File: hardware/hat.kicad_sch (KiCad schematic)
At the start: 41 parts

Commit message: schematic
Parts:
- C101: value (none) -> DSK-3R3H334T-HL; footprint (none) -> kicad-libraries:DSK
- C102, C103, C109, C111: value (none) -> 100nF; footprint (none) -> kicad-libraries:C0603F
- C104, C105, C106, C114, C115: value (none) -> 1uF; footprint (none) -> kicad-libraries:C0603F
- C107, C108, C110, C112, C113: value (none) -> 10uF; footprint (none) -> kicad-libraries:C1206
- C116, C117: value (none) -> DNP; footprint (none) -> kicad-libraries:C0402F
- D101: value (none) -> BAQ33-GS08; footprint (none) -> kicad-libraries:MiniMelf
- D102: value (none) -> blue; footprint (none) -> kicad-libraries:D0603F
- J101: value (none) -> Raspberry_Pi_2_3; footprint (none) -> kicad-libraries:raspberrypi_hat2
- J102: value (none) -> Boot; footprint (none) -> kicad-libraries:SolderJumper
- L101, L102: value (none) -> 742792040; footprint (none) -> kicad-libraries:R0805
- P101: value (none) -> Debug; footprint (none) -> kicad-libraries:DEBUG_PAD
- R101, R102, R103, R104, R106: value (none) -> 1k; footprint (none) -> kicad-libraries:R0603F
- R105: value (none) -> 68; footprint (none) -> kicad-libraries:R0603F
- RP101, RP105: value (none) -> 3.9k; footprint (none) -> kicad-libraries:4X0402
- RP102, RP103, RP104: value (none) -> 82; footprint (none) -> kicad-libraries:4X0402
- U101: value (none) -> XMC1100; footprint (none) -> QFN24-4x4mm-0.5mm
- U102: value (none) -> LD1117; footprint (none) -> kicad-libraries:SOT-223
- U103, U104: value (none) -> TPS22975; footprint (none) -> WSON8-2x2
- U105: value (none) -> PCF8523T; footprint (none) -> kicad-libraries:SO-8
- X101: value (none) -> 32.768kHz; footprint (none) -> kicad-libraries:AB26TRQ
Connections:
- net PowerGood: now reaches U101.20 (P0.9_IO)
- no-connect marks 26 -> 25
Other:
- note added: "Copyright Tinkerforge GmbH 2023. This documentation describes Open Hardware and is licensed under the CERN OHL v. 1.1. You may redistribute and modify this documentation under the terms of the CERN OHL v.1.1. (http://ohwr.org/cernohl). This documentation is distributed WITHOUT ANY EXPRESS OR IMPLIED WARRANTY, INCLUDING OF MERCHANTABILITY, SATISFACTORY QUALITY AND FITNESS FOR A PARTICULAR PURPOSE.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"
- note removed: "Copyright Tinkerforge GmbH 2021. This documentation describes Open Hardware and is licensed under the CERN OHL v. 1.1. You may redistribute and modify this documentation under the terms of the CERN OHL v.1.1. (http://ohwr.org/cernohl). This documentation is distributed WITHOUT ANY EXPRESS OR IMPLIED WARRANTY, INCLUDING OF MERCHANTABILITY, SATISFACTORY QUALITY AND FITNESS FOR A PARTICULAR PURPOSE.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"

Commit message: Proto V1.8
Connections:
- net GND: now also U101.16 (P0.5_IO)
- net PowerGood: now also U101.6 (P2.9_AI); no longer U101.20 (P0.9_IO)
- no-connect marks 25 -> 24
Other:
- note added: "Version Detect V1.8"

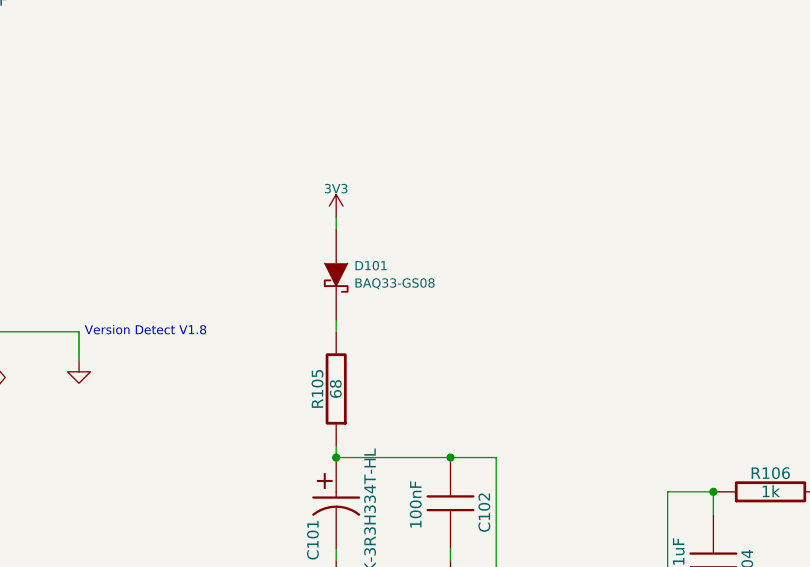
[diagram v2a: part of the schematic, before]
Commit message: changed D101
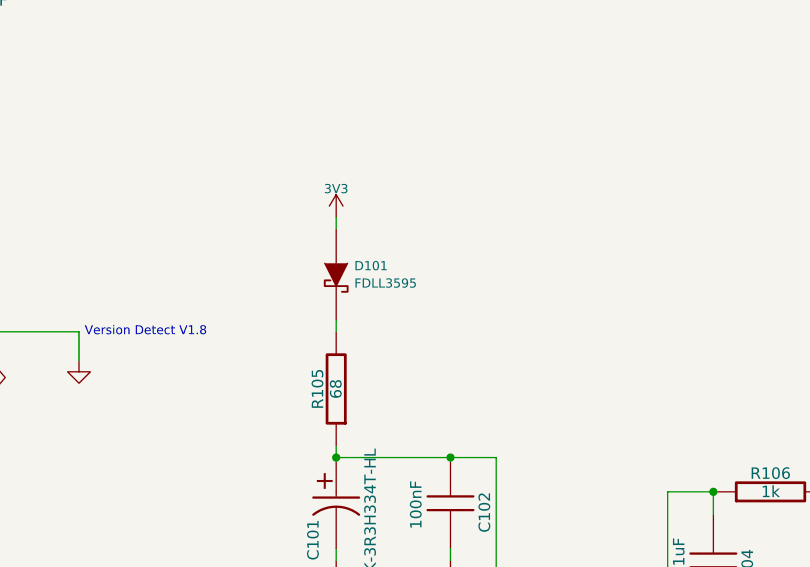
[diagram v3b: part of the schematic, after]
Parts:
- D101: value BAQ33-GS08 -> FDLL3595
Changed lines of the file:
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@@
       (effects (font (size 1.016 1.016)) (justify left))
     )
-    (property "Value" "BAQ33-GS08" (id 1) (at 94.7166 61.9252 90)
+    (property "Value" "FDLL3595" (id 1) (at 94.7166 61.9252 90)
       (effects (font (size 1.016 1.016)) (justify left))
     )
@@
     )
     (path "/00000000-0000-0000-0000-00005c8db5e2"
-      (reference "D101") (unit 1) (value "BAQ33-GS08") (footprint "kicad-libraries:MiniMelf")
+      (reference "D101") (unit 1) (value "FDLL3595") (footprint "kicad-libraries:MiniMelf")
     )
     (path "/00000000-0000-0000-0000-00005b476059"

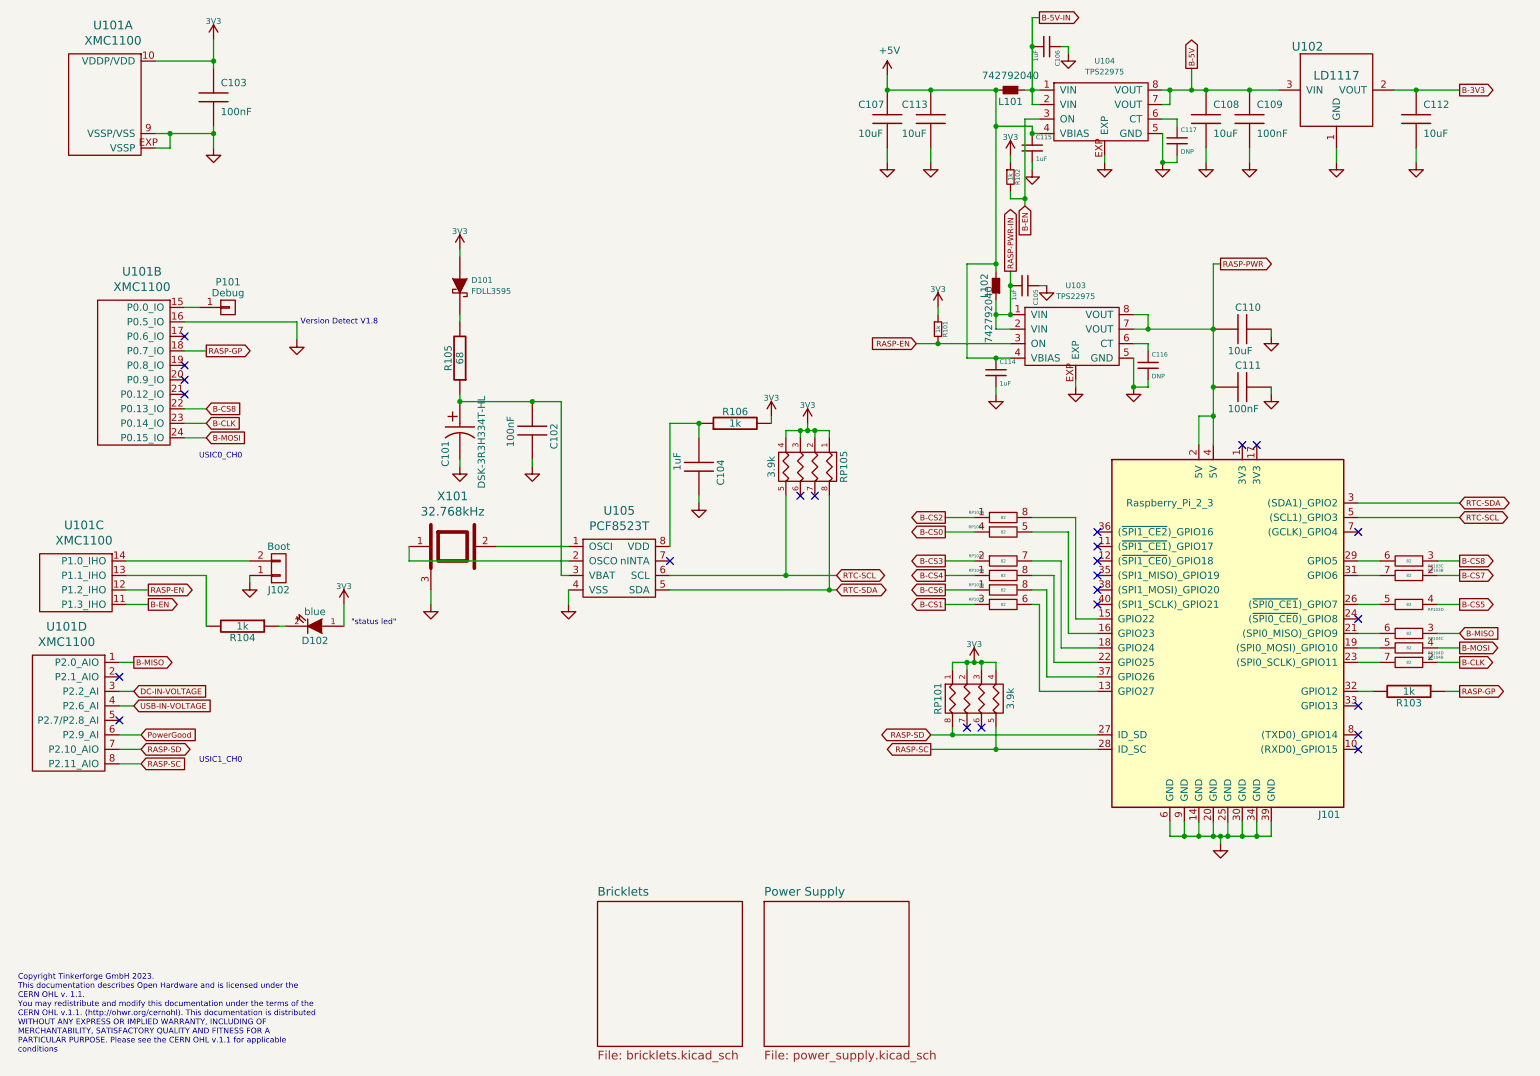
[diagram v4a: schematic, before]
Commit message: move to kicad 7
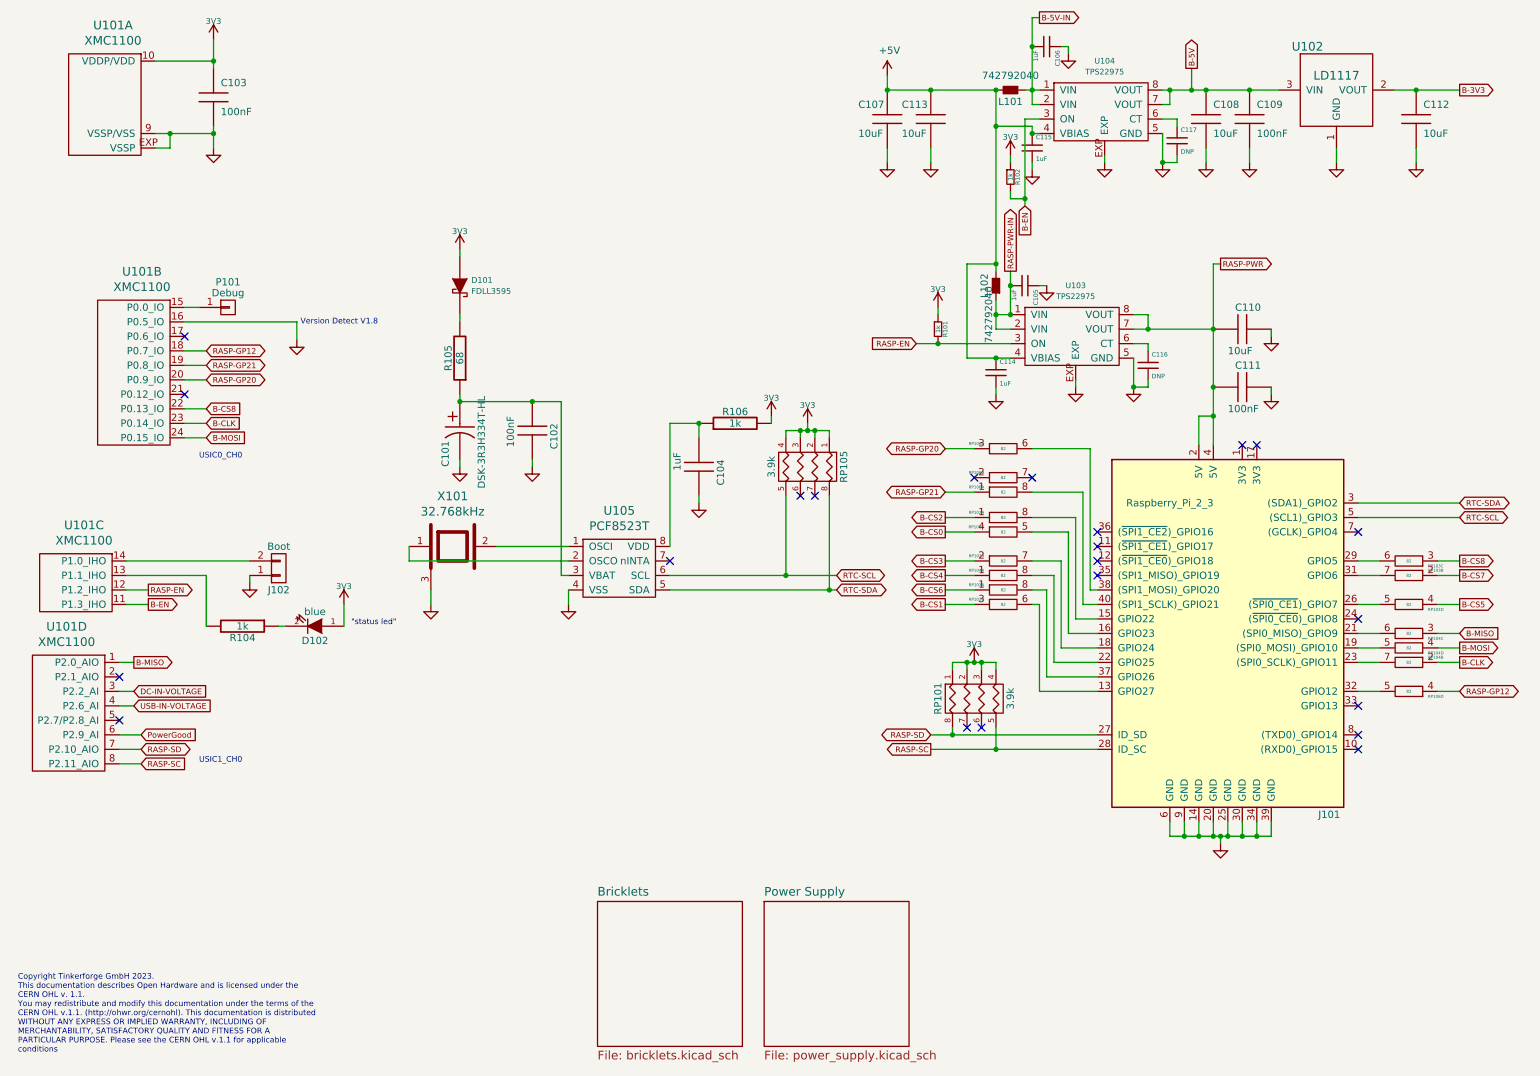
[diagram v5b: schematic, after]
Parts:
- removed R103: 1k, kicad-libraries:R0603F, symbol tinkerforge:R
- added RP106: 82, kicad-libraries:4X0402, symbol tinkerforge:R_PACK_SINGLE
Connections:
- net at J101.32 (GPIO12): now also RP106.5
- net at J101.38 ((SPI1_MOSI)_GPIO20): now also RP106.6
- net at J101.40 ((SPI1_SCLK)_GPIO21): now also RP106.8
- net RASP-GP21: now reaches U101.19 (P0.8_IO)
- net RASP-GP21: now also RP106.1
- net RASP-GP20: now reaches U101.20 (P0.9_IO)
- net RASP-GP20: now also RP106.3
- net RASP-GP renamed RASP-GP12
- net RASP-GP12: now also RP106.4
- no-connect marks 24 -> 22
